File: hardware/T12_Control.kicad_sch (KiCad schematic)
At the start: 52 parts, among them J1 Screw_Terminal_01x02, J2 GX12-5M, J3 SPI LCD, J4 I2C LCD, J5 SWD, J6 Serial, Q1 TPC8107, Q2 BC817, U1 SPX2954M3-3.3_SOT223, U2 24LC32, U3 SGM8551XN, U4 STM32F103CBTx

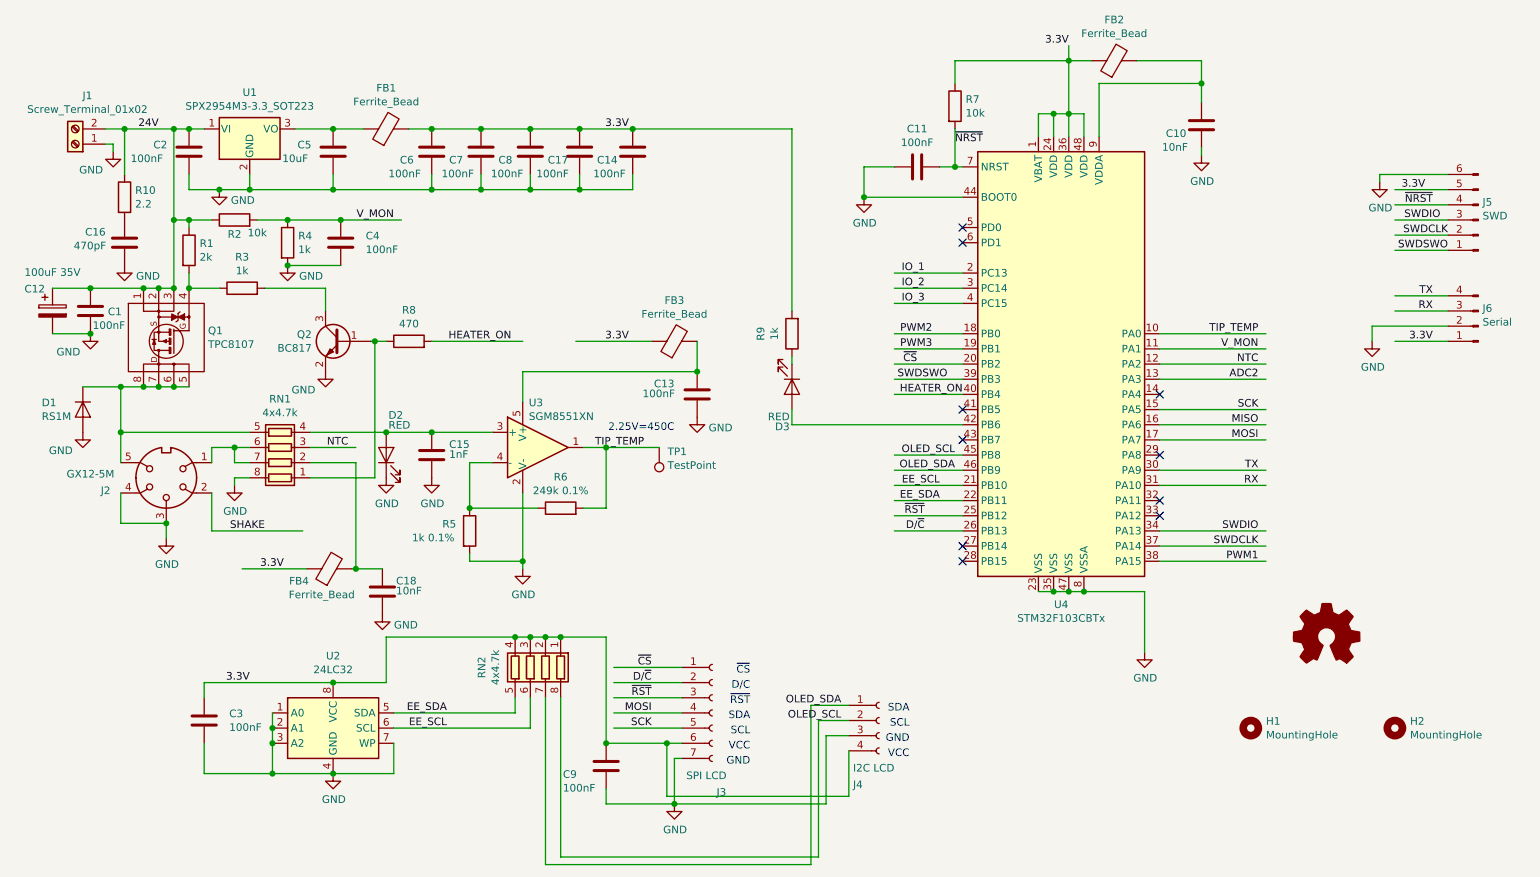
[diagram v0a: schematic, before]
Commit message: Update layout for power traces.
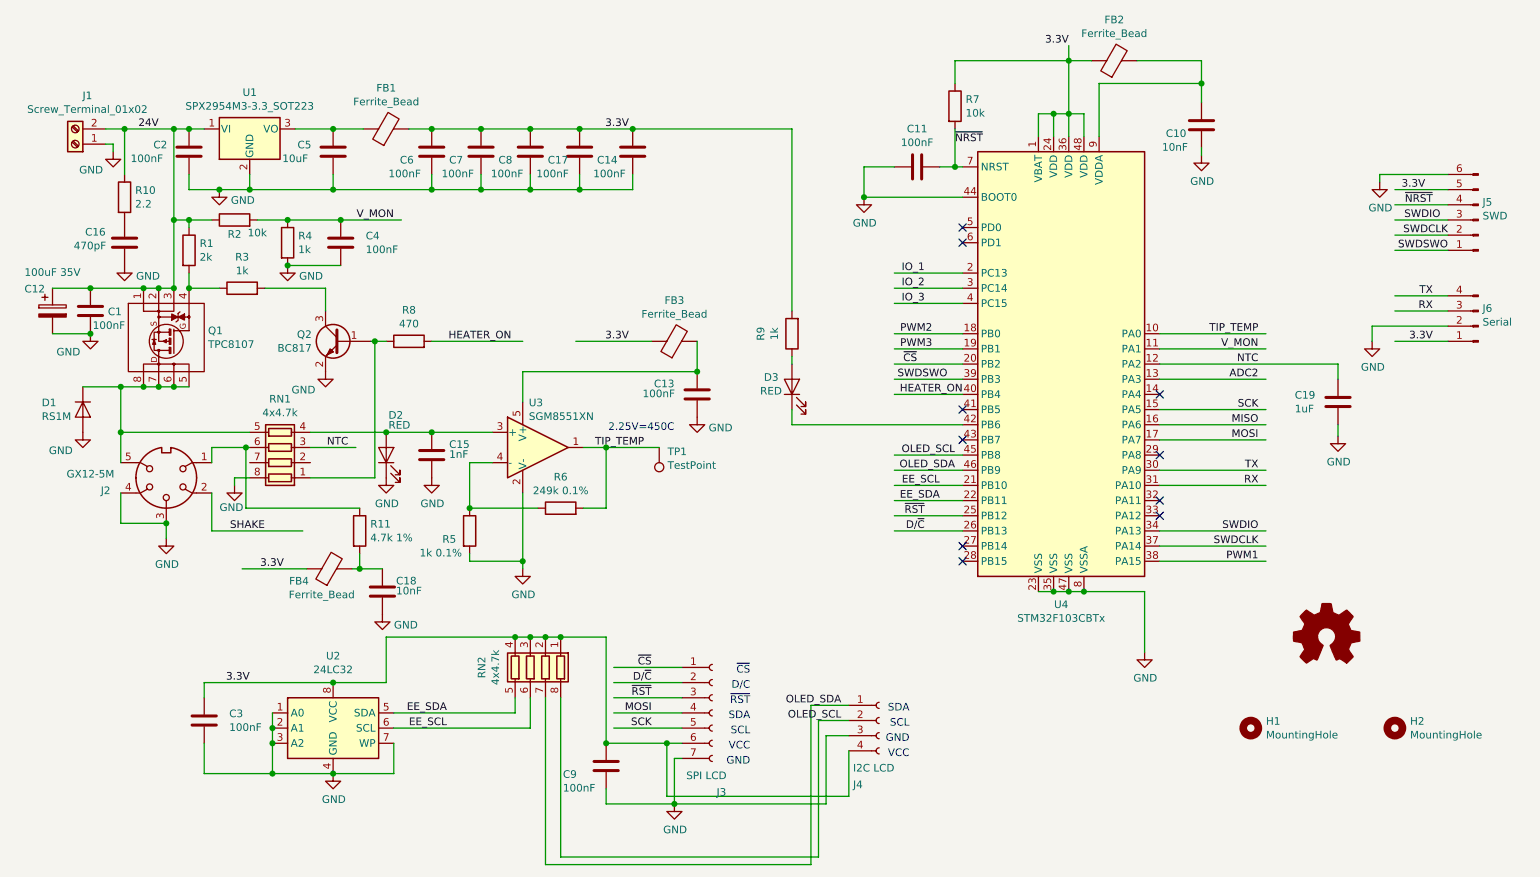
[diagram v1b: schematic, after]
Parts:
- added C19: 1uF, Capacitor_SMD:C_0603_1608Metric, symbol Device:C
- added R11: 4.7k 1%, Resistor_SMD:R_0603_1608Metric, symbol Device:R
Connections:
- net GND: now also C19.2
- net NTC: now also C19.1
- net at R9.1: now also D3.2 (A); no longer D3.1 (K)
- net at U4.42 (PB6): now also D3.1 (K); no longer D3.2 (A)
- net at C18.1, FB4.2: now also R11.2; no longer RN1.2 (R2.1)
- net at J2.1, RN1.6 (R3.2): now also R11.1; no longer RN1.7 (R2.2)
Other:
- moved on the sheet: D3

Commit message: Switch iron to 4 layer. Add dedicated GNDA signal.
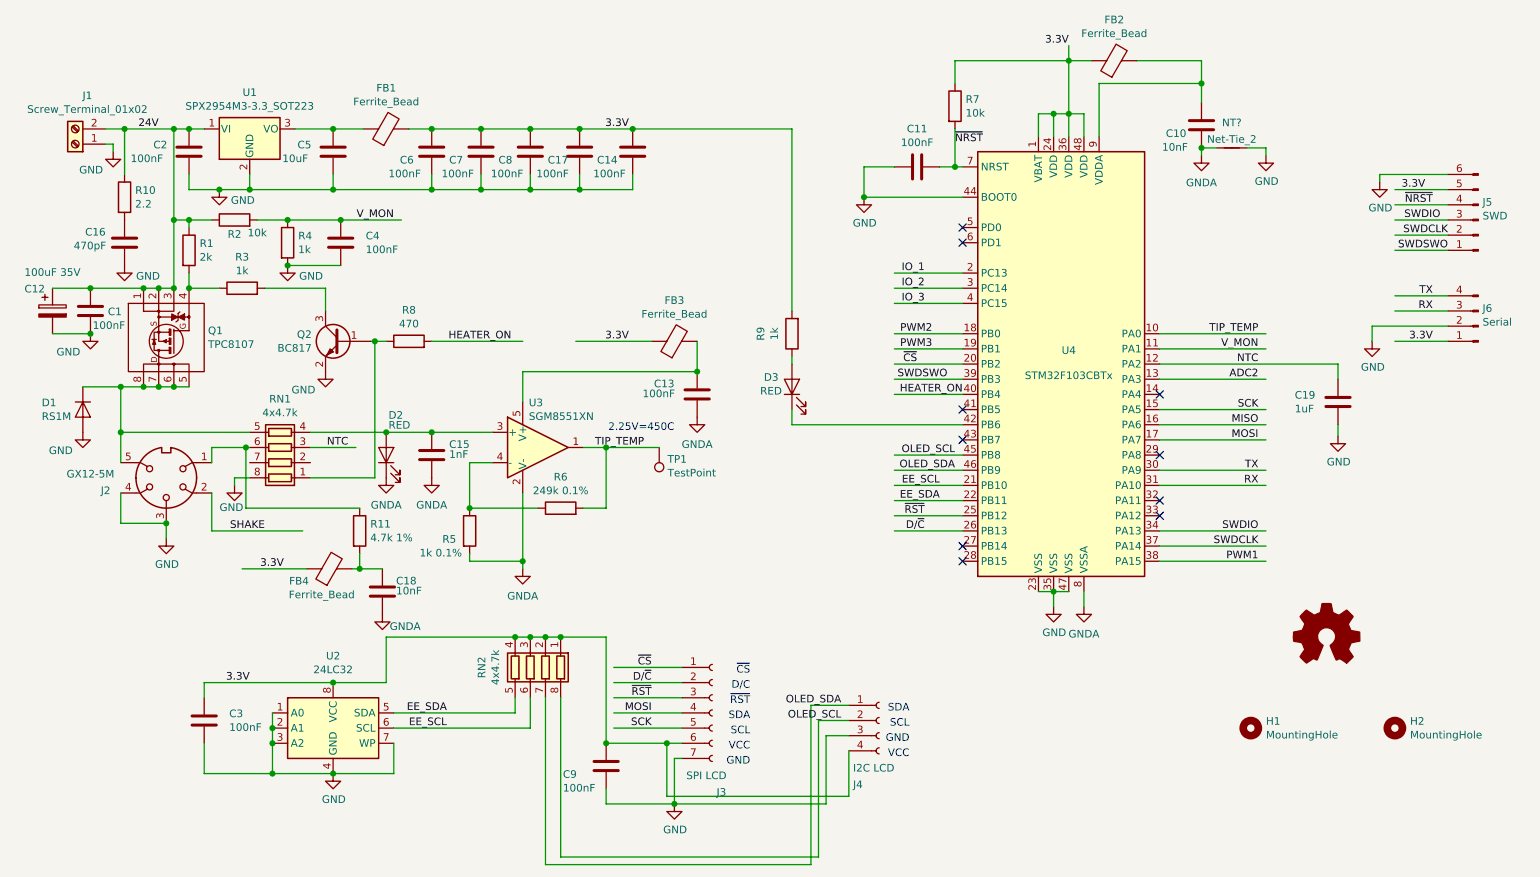
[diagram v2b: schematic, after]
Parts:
- added NT?: Net-Tie_2, NetTie:NetTie-2_SMD_Pad0.5mm, symbol Device:Net-Tie_2
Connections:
- net GND: now also NT?.2; no longer C10.2, C13.2, C15.2, C18.2, D2.1 (K), R5.2, U3.2 (V-), U4.8 (VSSA)
- net D/~C renamed D/~{C}
- net ~CS renamed ~{CS}
- net ~NRST renamed ~{NRST}
- net ~RST renamed ~{RST}
- new net GNDA: C10.2, C13.2, C15.2, C18.2, D2.1 (K), NT?.1, R5.2, U3.2 (V-), U4.8 (VSSA)
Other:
- note added: "~{CS}"
- note added: "~{RST}"
- note removed: "~CS"
- note removed: "~RST"

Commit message: Update Iron gerbers, start new Iron revision.
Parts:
- gave numbers to parts that had none: 1
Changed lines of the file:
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@@
   (symbol (lib_id "Device:Net-Tie_2") (at 215.265 48.895 0) (unit 1)
     (in_bom yes) (on_board yes) (fields_autoplaced)
-    (property "Reference" "NT?" (id 0) (at 215.265 44.6744 0))
+    (property "Reference" "NT1" (id 0) (at 215.265 44.6744 0))
     (property "Value" "Net-Tie_2" (id 1) (at 215.265 47.4495 0))
     (property "Footprint" "NetTie:NetTie-2_SMD_Pad0.5mm" (id 2) (at 215.265 48.895 0)
@@
   (symbol (lib_id "power:GNDA") (at 73.025 127 0) (unit 1)
     (in_bom yes) (on_board yes)
-    (property "Reference" "#PWR?" (id 0) (at 73.025 133.35 0)
+    (property "Reference" "#PWR0106" (id 0) (at 73.025 133.35 0)
       (effects (font (size 1.27 1.27)) hide)
     )
@@
   (symbol (lib_id "power:GNDA") (at 73.66 104.14 0) (unit 1)
     (in_bom yes) (on_board yes) (fields_autoplaced)
-    (property "Reference" "#PWR?" (id 0) (at 73.66 110.49 0)
+    (property "Reference" "#PWR0104" (id 0) (at 73.66 110.49 0)
       (effects (font (size 1.27 1.27)) hide)
     )
@@
   (symbol (lib_id "power:GNDA") (at 81.28 104.14 0) (unit 1)
     (in_bom yes) (on_board yes) (fields_autoplaced)
-    (property "Reference" "#PWR?" (id 0) (at 81.28 110.49 0)
+    (property "Reference" "#PWR0105" (id 0) (at 81.28 110.49 0)
       (effects (font (size 1.27 1.27)) hide)
     )
@@
   (symbol (lib_id "power:GNDA") (at 96.52 119.38 0) (unit 1)
     (in_bom yes) (on_board yes) (fields_autoplaced)
-    (property "Reference" "#PWR?" (id 0) (at 96.52 125.73 0)
+    (property "Reference" "#PWR0108" (id 0) (at 96.52 125.73 0)
       (effects (font (size 1.27 1.27)) hide)
     )
@@
   (symbol (lib_id "power:GNDA") (at 125.73 93.98 0) (unit 1)
     (in_bom yes) (on_board yes) (fields_autoplaced)
-    (property "Reference" "#PWR?" (id 0) (at 125.73 100.33 0)
+    (property "Reference" "#PWR0107" (id 0) (at 125.73 100.33 0)
       (effects (font (size 1.27 1.27)) hide)
     )
@@
   (symbol (lib_id "power:GNDA") (at 190.5 125.73 0) (unit 1)
     (in_bom yes) (on_board yes) (fields_autoplaced)
-    (property "Reference" "#PWR?" (id 0) (at 190.5 132.08 0)
+    (property "Reference" "#PWR0101" (id 0) (at 190.5 132.08 0)
       (effects (font (size 1.27 1.27)) hide)
     )
@@
   (symbol (lib_id "power:GNDA") (at 210.185 50.165 0) (unit 1)
     (in_bom yes) (on_board yes) (fields_autoplaced)
-    (property "Reference" "#PWR?" (id 0) (at 210.185 56.515 0)
+    (property "Reference" "#PWR0102" (id 0) (at 210.185 56.515 0)
       (effects (font (size 1.27 1.27)) hide)
     )
@@
   (symbol (lib_id "power:GND") (at 220.98 50.165 0) (unit 1)
     (in_bom yes) (on_board yes)
-    (property "Reference" "#PWR?" (id 0) (at 220.98 56.515 0)
+    (property "Reference" "#PWR0103" (id 0) (at 220.98 56.515 0)
       (effects (font (size 1.27 1.27)) hide)
     )
@@
       (reference "#PWR022") (unit 1) (value "GND") (footprint "")
     )
+    (path "/e4b48998-ef2c-4bfc-b002-b0c77bddc7bd"
+      (reference "#PWR0101") (unit 1) (value "GNDA") (footprint "")
+    )
+    (path "/4c25c283-98d7-4c49-a2fb-60c8f35740ca"
+      (reference "#PWR0102") (unit 1) (value "GNDA") (footprint "")
+    )
+    (path "/ad2891c8-e9cb-4ae9-ae39-4abcf598ec6d"
+      (reference "#PWR0103") (unit 1) (value "GND") (footprint "")
+    )
+    (path "/cd2e13a1-9cf9-4799-9e46-4de4068044ba"
+      (reference "#PWR0104") (unit 1) (value "GNDA") (footprint "")
+    )
     (path "/2ef7d185-095e-4dcc-9fea-dd7eb5300d0a"
-      (reference "#PWR?") (unit 1) (value "GNDA") (footprint "")
+      (reference "#PWR0105") (unit 1) (value "GNDA") (footprint "")
+    )
+    (path "/f6262686-5ba7-4b6a-8a67-eb21a9d6a639"
+      (reference "#PWR0106") (unit 1) (value "GNDA") (footprint "")
+    )
+    (path "/76310b34-c88e-4022-aa1b-907b01936166"
+      (reference "#PWR0107") (unit 1) (value "GNDA") (footprint "")
     )
     (path "/3ed42bf3-00b6-4264-8e37-5862b7930fc7"
-      (reference "#PWR?") (unit 1) (value "GNDA") (footprint "")
-    )
-    (path "/4c25c283-98d7-4c49-a2fb-60c8f35740ca"
-      (reference "#PWR?") (unit 1) (value "GNDA") (footprint "")
-    )
-    (path "/76310b34-c88e-4022-aa1b-907b01936166"
-      (reference "#PWR?") (unit 1) (value "GNDA") (footprint "")
-    )
-    (path "/ad2891c8-e9cb-4ae9-ae39-4abcf598ec6d"
-      (reference "#PWR?") (unit 1) (value "GND") (footprint "")
-    )
-    (path "/cd2e13a1-9cf9-4799-9e46-4de4068044ba"
-      (reference "#PWR?") (unit 1) (value "GNDA") (footprint "")
-    )
-    (path "/e4b48998-ef2c-4bfc-b002-b0c77bddc7bd"
-      (reference "#PWR?") (unit 1) (value "GNDA") (footprint "")
-    )
-    (path "/f6262686-5ba7-4b6a-8a67-eb21a9d6a639"
-      (reference "#PWR?") (unit 1) (value "GNDA") (footprint "")
+      (reference "#PWR0108") (unit 1) (value "GNDA") (footprint "")
     )
     (path "/e7da8b02-dc3d-450d-8850-7f0461ca49ca"
@@
     )
     (path "/75366d49-4904-4b92-b0b0-4e597f131c1b"
-      (reference "NT?") (unit 1) (value "Net-Tie_2") (footprint "NetTie:NetTie-2_SMD_Pad0.5mm")
+      (reference "NT1") (unit 1) (value "Net-Tie_2") (footprint "NetTie:NetTie-2_SMD_Pad0.5mm")
     )
     (path "/0d2a404f-024a-4ffe-b0c5-80a1d2737d76"
